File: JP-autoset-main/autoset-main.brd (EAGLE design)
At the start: 68.6 x 53.3 mm, 120 parts, among them J1 TERM_1X2_0.1, J10 TERM_1X2_0.1, J11 TERM_1X2_0.1, J12 TERM_1X2_0.1, J2 TERM_1X6_0.1, J3 TERM_1X2_0.1, J4 TERM_1X4_0.1, J5 TERM_1X2_0.1, J6 TERM_1X2_0.1, J7 TERM_1X2_0.1, J8 TERM_1X2_0.1, J9 TERM_1X2_0.1, P1 RECT_1X8, P2 RECT_1X6, P3 RECT_1X8, P4 RECT_1X10, Q1 NMOS-RUC002N05, Q2 NMOS-RUC002N05, Q3 NMOS-RUC002N05, Q4 NMOS-RUC002N05, Q5 NMOS-RUC002N05, Q7 PMOS-FQD7P06TM, U1 LM293DT, U10 QRE1113GR, U2 LM293DT, U3 QRE1113GR, U4 QRE1113GR, U5 QRE1113GR, U6 LD1085CDT-R, U8 A3909

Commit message: Multiple updates
Library update (add switch)
Updated sensing board to 4 layers, added some filtering.
Updated control board to 4 layers, added functionality.
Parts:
- removed D3, D4, D5, D6: LED, dsantoro-discrete:L0805
- removed Z17: NC, dsantoro-dir:NC_TH
- added R56: 0, dsantoro-discrete:R0603
- added SW1: GPTS203211B, dsantoro-sw:GPTS203211B
- moved R51 464.6 mm to (33.0, 58.4), flipped to the bottom, turned to 180 degrees
- moved R49 431.1 mm to (54.3, 58.4), turned to 180 degrees
- moved C23 404.2 mm to (3.49, 6.67)
- moved R50 402.4 mm to (1.59, 4.76), flipped to the bottom, turned to 90 degrees
- moved Q5 396.2 mm to (4.13, 5.08), flipped to the bottom, turned to 180 degrees
- moved R40 394.0 mm to (37.5, 58.4), flipped to the bottom
- moved J8 384.2 mm to (1.59, 1.91), turned to 90 degrees
- moved C19 368.8 mm to (19.7, 6.67), flipped to the bottom
- moved R45 366.1 mm to (19.7, 4.13), flipped to the bottom, turned to 180 degrees
- moved Q4 358.7 mm to (22.9, 2.54), flipped to the bottom, turned to 270 degrees
- moved R55 349.6 mm to (12.4, 57.5), flipped to the bottom, turned to 90 degrees
- moved J7 348.8 mm to (16.8, 1.91), turned to 90 degrees
- moved C27 346.5 mm to (12.4, 54.3), flipped to the bottom, turned to 270 degrees
- moved C16 340.4 mm to (8.89, 14.0), flipped to the bottom
- moved J12 339.7 mm to (10.2, 55.2)
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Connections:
- net BUTTON1: now also P3.2; no longer P3.3
- net BUTTON2: now also P3.3; no longer P3.2
- net LED1: now also P4.9; no longer P3.4
- net LED2: now also P4.8; no longer P4.7
- net LED3: now also P3.4; no longer P4.9
- net LED4: now also P4.7; no longer P4.8
- net N$12: no longer D3.2
- net N$14: no longer D3.1
- net N$16: no longer D4.1
- net N$18: no longer D5.2
- net N$19: no longer D5.1
- net N$20: no longer D6.2
- net N$23: no longer D6.1
- net N$4: no longer D4.2
- net N$5: now also R56.1, R7.2, R8.2, SW1.1; no longer P2.6, Z17.P$1
- net VCC: no longer C15.1, C16.1, C19.1, C23.1, R38.2, R39.2, R45.2, R50.2, R52.2, R53.2, R54.2, R55.2
- net VCOPT1: now also P2.1; no longer P2.4
- net VCOPT2: now also P2.2; no longer P2.3
- net VCOPT3: now also P2.3; no longer P2.2
- net VCOPT4: now also P2.4; no longer P2.1
- net VDD: now also C15.1, C16.1, C19.1, C23.1, R38.2, R39.2, R45.2, R50.2, R52.2, R53.2, R54.2, R55.2, R56.2, SW1.2; no longer R7.2, R8.2
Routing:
- net LED4: track 0.00 -> 80.7 mm
- net LED3: track 0.00 -> 79.2 mm
- net LED1: track 0.00 -> 72.0 mm
- net LED2: track 0.00 -> 64.9 mm
- net VDD: track 8.78 -> 67.9 mm, vias 0 -> 47
- net BUTTON1: track 0.00 -> 54.6 mm
- net BUTTON3: track 0.00 -> 53.1 mm
- net BUTTON2: track 0.00 -> 48.9 mm
- net BUTTON4: track 0.00 -> 41.4 mm
- net GND: track 57.3 -> 95.0 mm, vias 37 -> 130
- net N$5: track 3.17 -> 38.4 mm
- net VCC: track 44.0 -> 10.7 mm
- net VOPT2: track 71.7 -> 59.3 mm
- net VOPT4: track 56.1 -> 44.9 mm
- net VOPT1: track 72.3 -> 61.4 mm
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- added copper zone on layer 2, net GND
- added copper zone on layer 15, net VDD
- removed copper zone on layer 16, net GND
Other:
- board size 68.6 x 53.3 mm -> 68.6 x 63.5 mm
- board text added: "0x10C33901"
- board text added: "MOTOR CONTROL / SENSORS / INTERFACE. REV. 2."
- board text removed: "0x10B33900"
- board text removed: "MOTOR CONTROL / SENSORS/ INTERFACE. REV. 1."

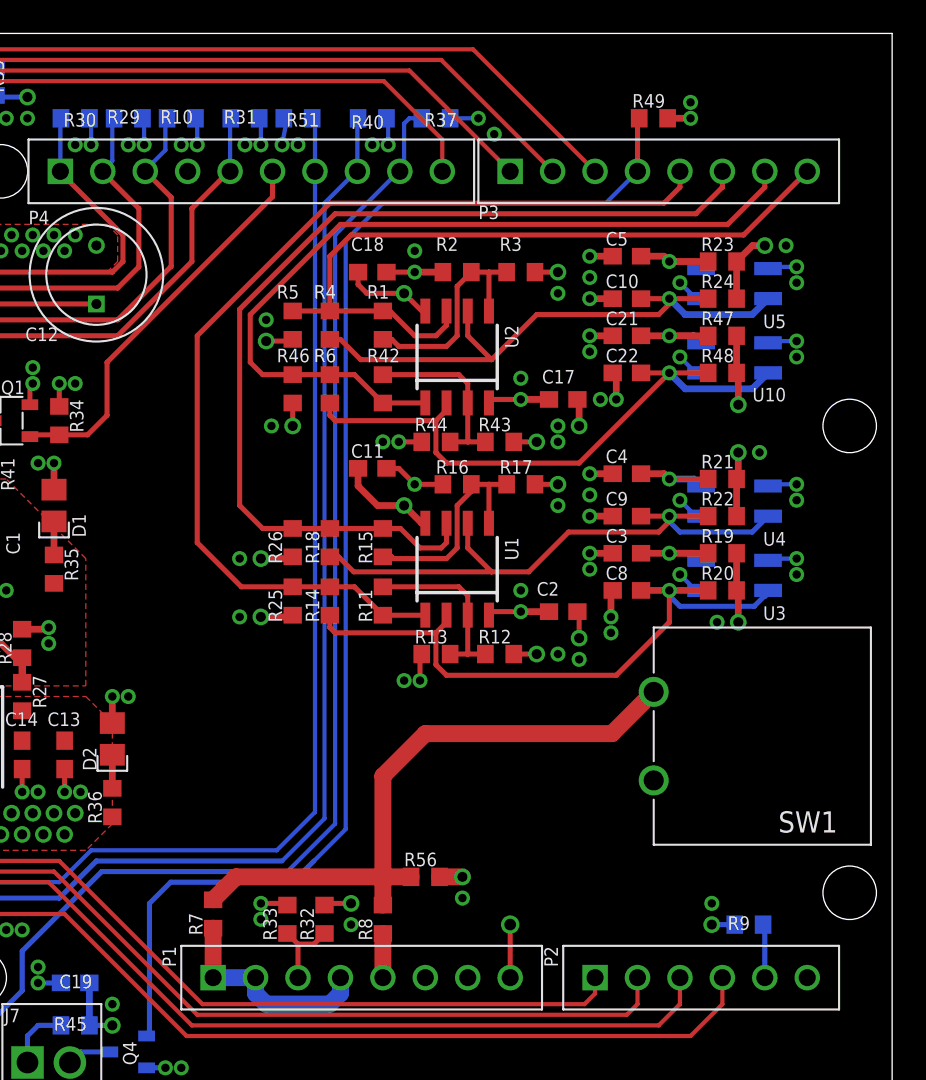
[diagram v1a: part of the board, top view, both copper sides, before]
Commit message: Updates
Sensing manufacture. Updated library. Updated main schematic to include
magnetic sensor.
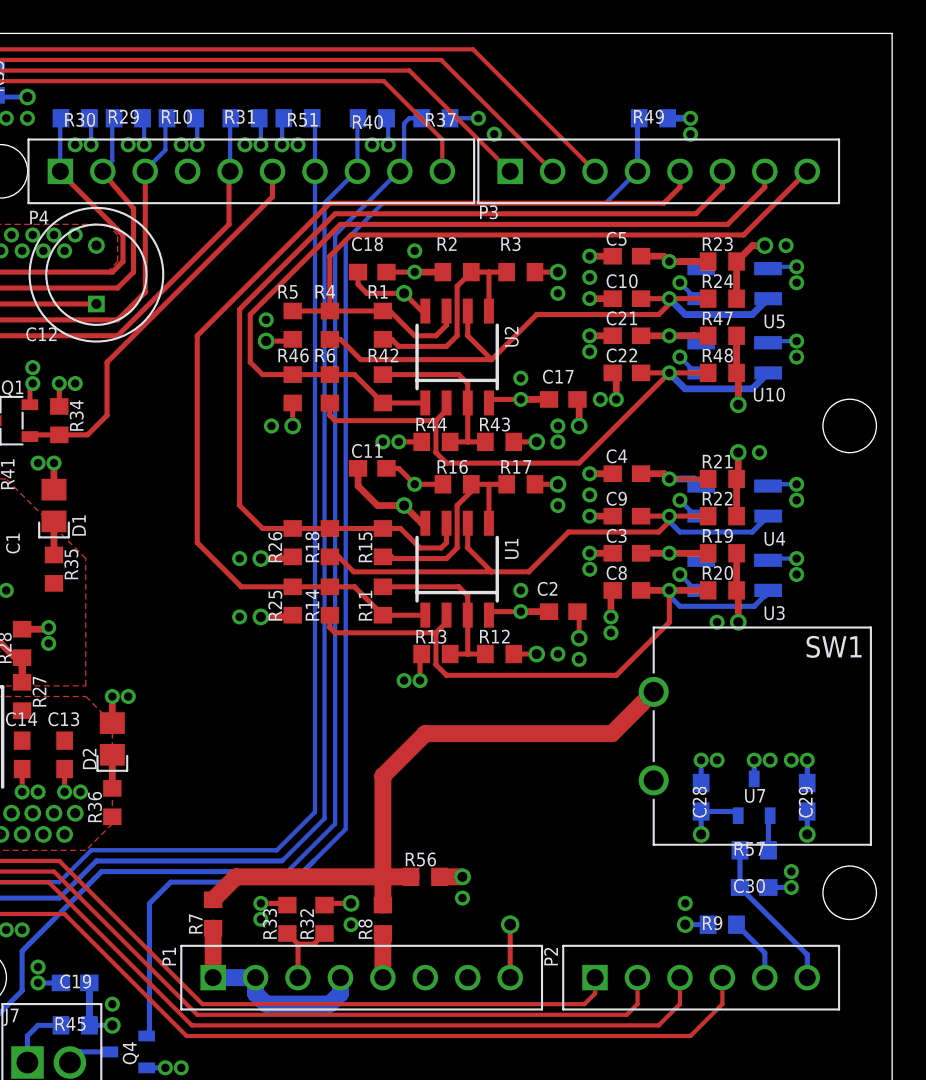
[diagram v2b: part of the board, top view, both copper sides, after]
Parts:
- added C28, C29, C30: 0.1u, dsantoro-discrete:C0603
- added R57: 200, dsantoro-discrete:R0603
- added U7: DRV5053, dsantoro-sens:SOT23
- moved R9 1.59 mm to (58.4, 10.2)
- flipped R49 to the bottom, turned to 0 degrees
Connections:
- new net N$25: R57.1, U7.2
- new net VMAG: C30.1, P2.6, R57.2
- net GND: now also C28.2, C29.2, C30.2, U7.3
- net VDD: now also C28.1, C29.1, U7.1
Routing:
- net VMAG: track 0.00 -> 9.29 mm
- net VDD: track 67.9 -> 73.2 mm, vias 47 -> 49
- net GND: track 95.0 -> 99.9 mm, vias 130 -> 138
- net N$25: track 0.00 -> 2.18 mm
- net MPWM2: track 23.4 -> 22.2 mm
- net N$24: track 3.22 -> 3.88 mm

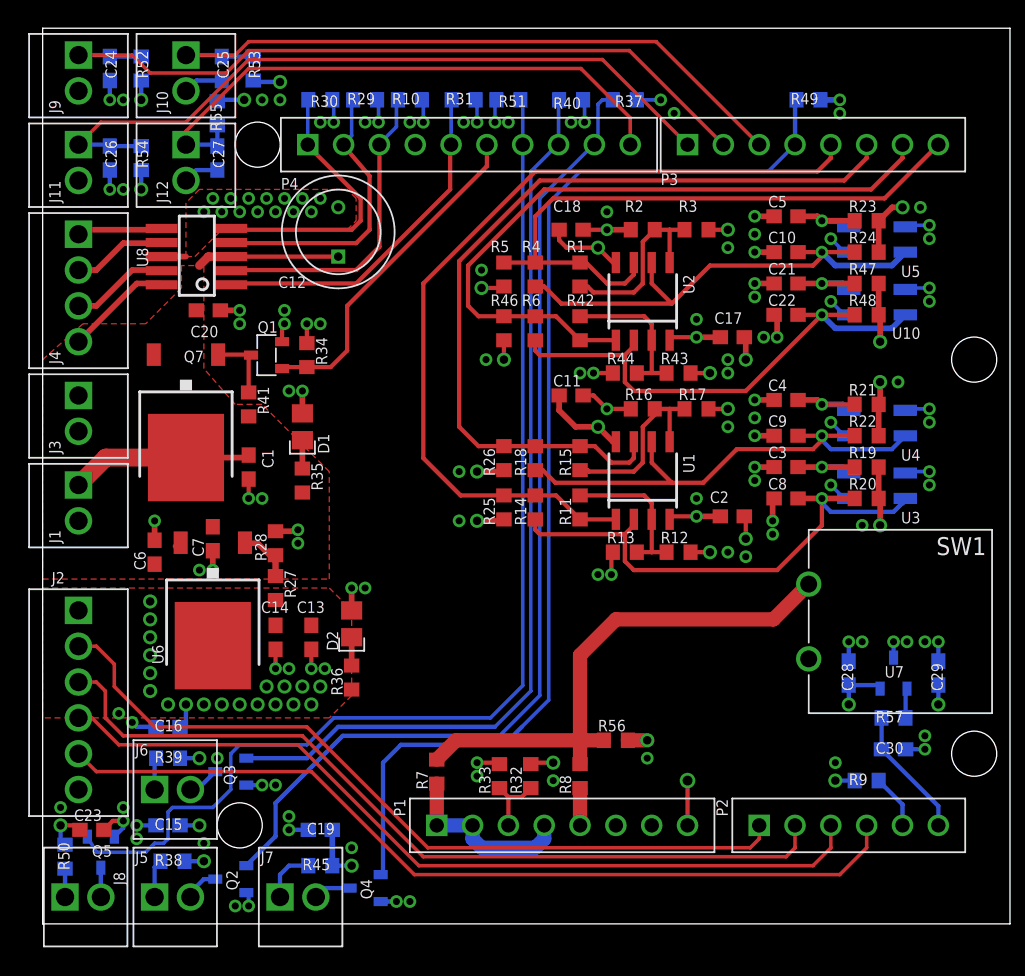
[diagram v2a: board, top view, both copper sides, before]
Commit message: Main Board Updates
Move things away from holes.  Create mfg files
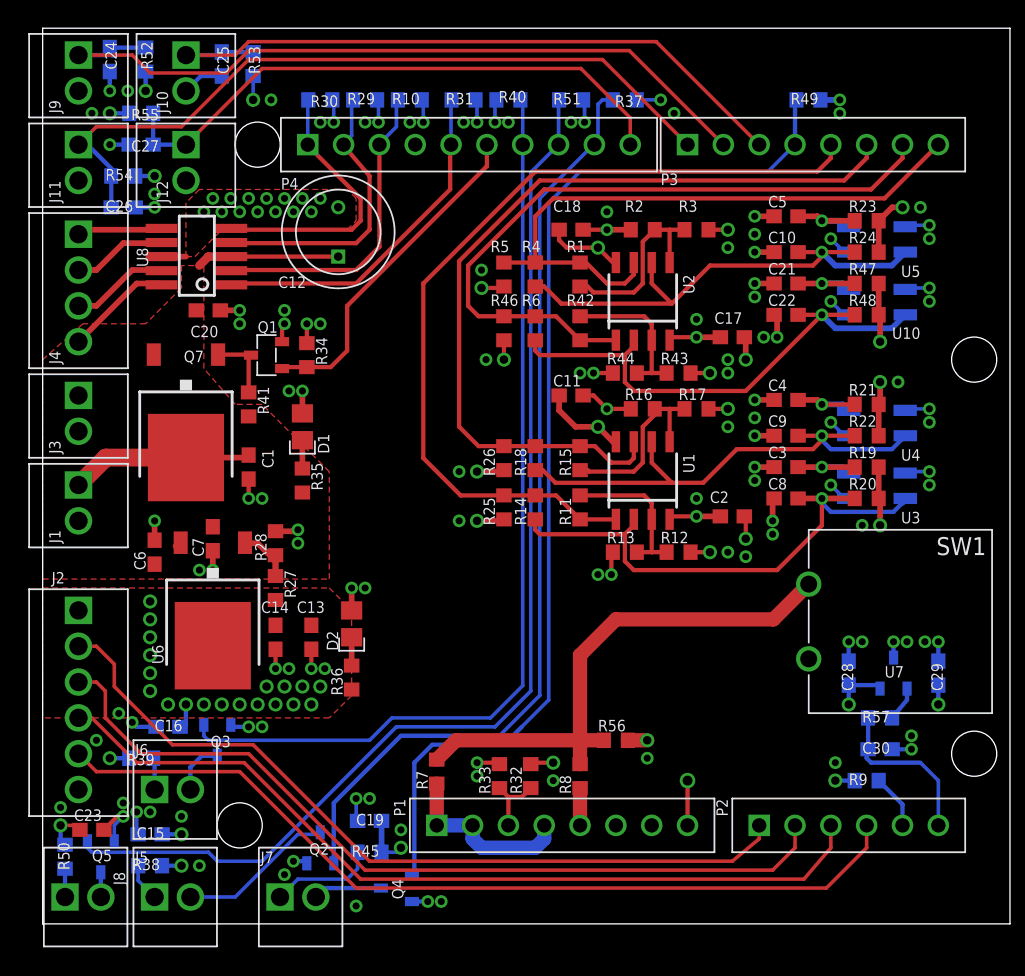
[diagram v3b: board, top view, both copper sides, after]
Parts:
- moved Q2 6.73 mm to (19.7, 5.40), turned to 0 degrees
- moved C27 5.48 mm to (6.99, 55.2), turned to 0 degrees
- moved R55 5.40 mm to (6.99, 57.5), turned to 0 degrees
- moved R40 4.45 mm to (33.0, 58.4), turned to 180 degrees
- moved R51 4.45 mm to (37.5, 58.4), turned to 0 degrees
- moved C26 3.62 mm to (5.71, 50.8), turned to 180 degrees
- moved R45 3.62 mm to (23.2, 5.08)
- moved C19 3.55 mm to (23.2, 7.30)
- moved Q3 2.42 mm to (12.4, 13.0), turned to 180 degrees
- moved Q4 2.22 mm to (25.1, 2.54)
- moved R39 1.91 mm to (6.99, 11.7), turned to 0 degrees
- moved R54 1.80 mm to (5.71, 53.0), turned to 180 degrees
- moved R38 1.62 mm to (7.62, 4.13)
- moved C15 1.42 mm to (7.62, 6.35)
- moved C30 0.95 mm to (59.4, 12.4)
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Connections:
- net LED2: now also P4.7; no longer P4.8
- net LED4: now also P4.8; no longer P4.7
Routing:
- net N$12: track 2.47 -> 11.1 mm
- net LED1: track 72.0 -> 66.9 mm
- net N$19: track 3.86 -> 7.50 mm
- net VMAG: track 9.29 -> 11.8 mm
- net N$18: track 2.66 -> 4.88 mm
- net LED3: track 79.2 -> 77.0 mm
- net LED2: track 64.9 -> 66.8 mm
- net N$4: track 2.28 -> 3.83 mm
- net BUTTON3: track 53.1 -> 54.2 mm
- net VDD: track 73.2 -> 72.2 mm
- net VCOPT3: track 59.8 -> 60.7 mm
- net VCOPT2: track 58.9 -> 59.7 mm
- net VCOPT4: track 61.8 -> 62.6 mm
- net VCOPT1: track 56.3 -> 57.0 mm
- net GND: track 99.9 -> 100.6 mm, vias 138 -> 141
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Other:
- board text added: "MOTOR CONTROL/SENSORS/INTERFACE. REV. 2."
- board text removed: "MOTOR CONTROL / SENSORS / INTERFACE. REV. 2."
